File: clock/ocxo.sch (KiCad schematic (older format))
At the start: 50 parts, among them Q201 MMBT3904, U201 PCA9306, U202 DAC8830, U203 LMV722, U204 LTC2990, U205 LP3853, U207 NC7SZ125, Y202 CX210

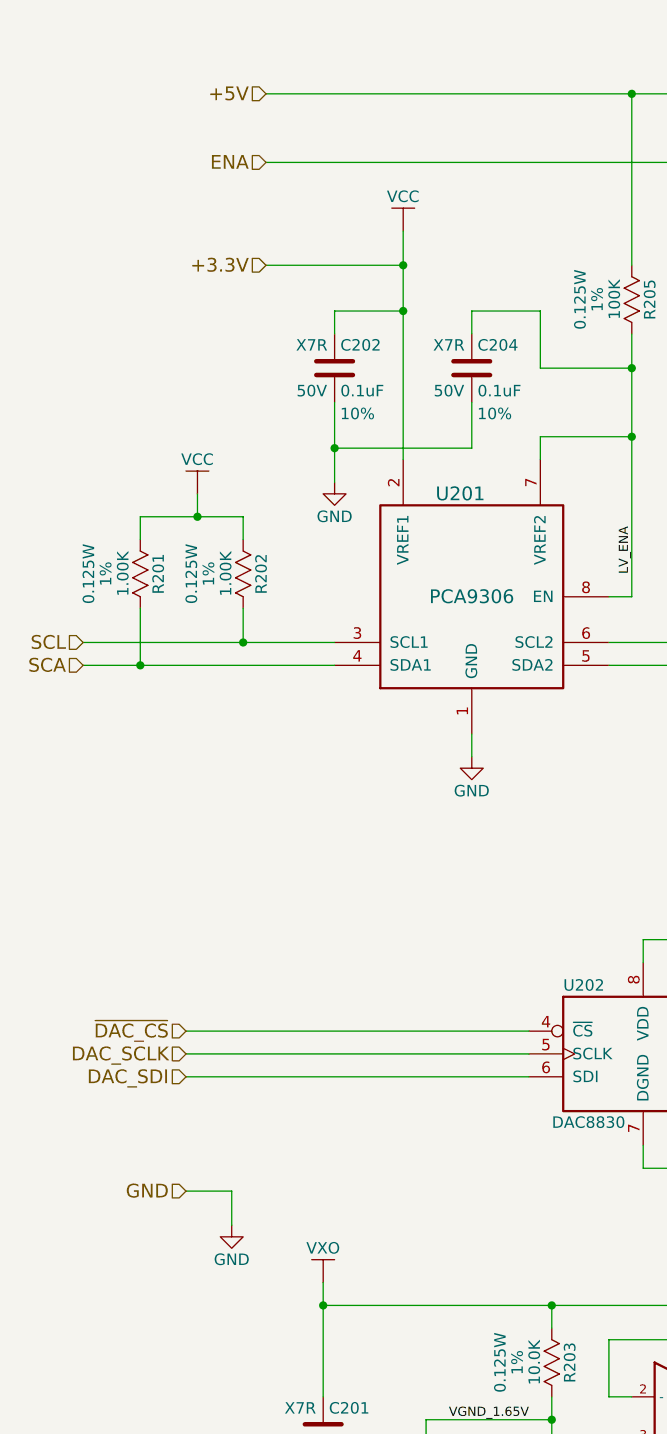
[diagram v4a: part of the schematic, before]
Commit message: Remove sheet to sheet power interconnect because power symbols are global.
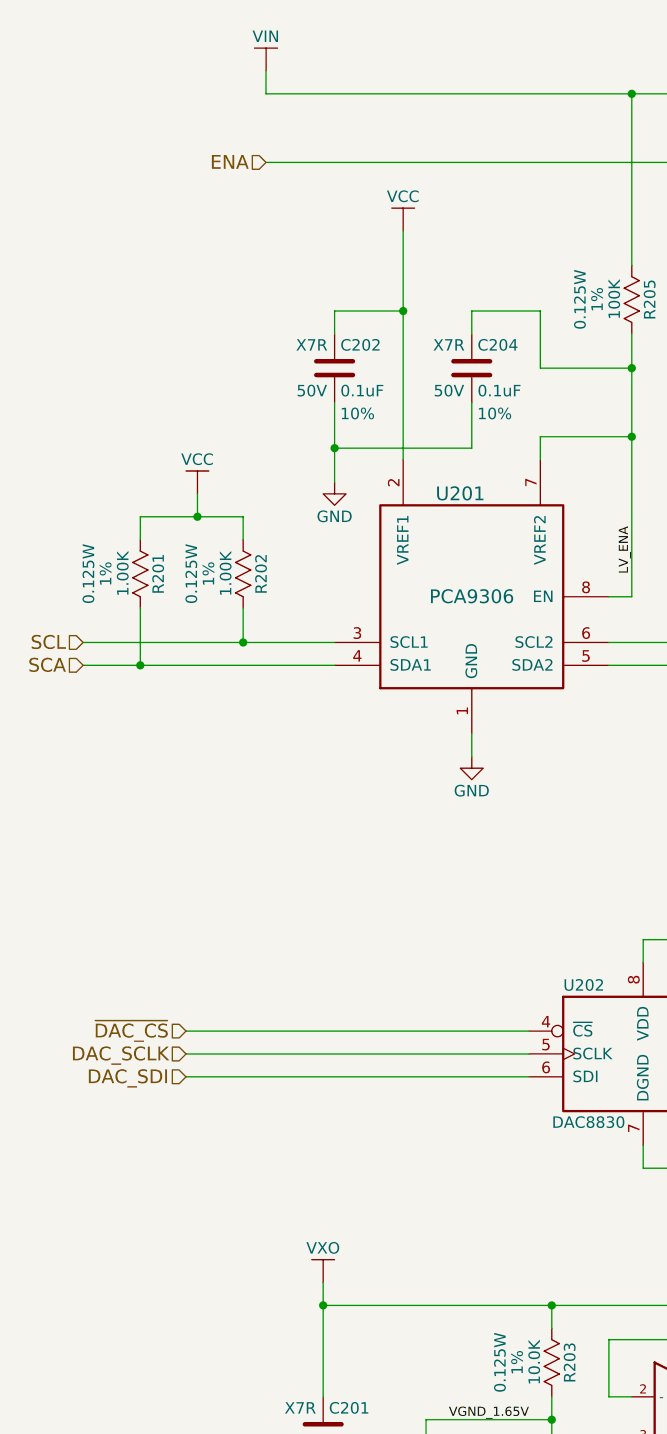
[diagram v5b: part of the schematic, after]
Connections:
- net +5V renamed VIN
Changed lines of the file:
@@
 Comment4 ""
 $EndDescr
-Text HLabel 1650 1000 0    60   Input ~ 0
-+5V
-Text HLabel 1300 5800 0    60   Input ~ 0
-GND
-$Comp
-L GND #PWR222
+$Comp
+L GND #PWR010
 U 1 1 5622D09D
 P 8800 2250
-F 0 "#PWR222" H 8800 2000 50  0001 C CNN
+F 0 "#PWR010" H 8800 2000 50  0001 C CNN
 F 1 "GND" H 8800 2100 50  0000 C CNN
 F 2 "" H 8800 2250 60  0000 C CNN
@@
 	1    0    0    -1
 $EndComp
-Text HLabel 1650 1750 0    60   Input ~ 0
-+3.3V
 Text HLabel 850  3400 0    60   Input ~ 0
 SCL
@@
 ENA
 $Comp
-L GND #PWR204
+L GND #PWR011
 U 1 1 5622E675
 P 1950 2700
-F 0 "#PWR204" H 1950 2450 50  0001 C CNN
+F 0 "#PWR011" H 1950 2450 50  0001 C CNN
 F 1 "GND" H 1950 2550 50  0000 C CNN
 F 2 "" H 1950 2700 60  0000 C CNN
@@
 $EndComp
 $Comp
-L GND #PWR211
+L GND #PWR012
 U 1 1 5622EAE9
 P 4750 2300
-F 0 "#PWR211" H 4750 2050 50  0001 C CNN
+F 0 "#PWR012" H 4750 2050 50  0001 C CNN
 F 1 "GND" H 4750 2150 50  0000 C CNN
 F 2 "" H 4750 2300 60  0000 C CNN
@@
 $EndComp
 $Comp
-L GND #PWR213
+L GND #PWR013
 U 1 1 5622ED34
 P 5500 3500
-F 0 "#PWR213" H 5500 3250 50  0001 C CNN
+F 0 "#PWR013" H 5500 3250 50  0001 C CNN
 F 1 "GND" H 5500 3350 50  0000 C CNN
 F 2 "" H 5500 3500 60  0000 C CNN
@@
 $EndComp
 $Comp
-L GND #PWR206
+L GND #PWR014
 U 1 1 5622EF10
 P 2550 3900
-F 0 "#PWR206" H 2550 3650 50  0001 C CNN
+F 0 "#PWR014" H 2550 3650 50  0001 C CNN
 F 1 "GND" H 2550 3750 50  0000 C CNN
 F 2 "" H 2550 3900 60  0000 C CNN
@@
 $EndComp
 $Comp
-L GND #PWR212
+L GND #PWR015
 U 1 1 5622FB6A
 P 4750 7550
-F 0 "#PWR212" H 4750 7300 50  0001 C CNN
+F 0 "#PWR015" H 4750 7300 50  0001 C CNN
 F 1 "GND" H 4750 7400 50  0000 C CNN
 F 2 "" H 4750 7550 60  0000 C CNN
@@
 $EndComp
 $Comp
-L GND #PWR208
+L GND #PWR016
 U 1 1 56230FF6
 P 3500 5800
-F 0 "#PWR208" H 3500 5550 50  0001 C CNN
+F 0 "#PWR016" H 3500 5550 50  0001 C CNN
 F 1 "GND" H 3500 5650 50  0000 C CNN
 F 2 "" H 3500 5800 60  0000 C CNN
@@
 $EndComp
 $Comp
-L GND #PWR219
+L GND #PWR017
 U 1 1 5623121C
 P 7750 6200
-F 0 "#PWR219" H 7750 5950 50  0001 C CNN
+F 0 "#PWR017" H 7750 5950 50  0001 C CNN
 F 1 "GND" H 7750 6050 50  0000 C CNN
 F 2 "" H 7750 6200 60  0000 C CNN
@@
 $EndComp
 $Comp
-L GND #PWR215
+L GND #PWR018
 U 1 1 56231287
 P 5850 6100
-F 0 "#PWR215" H 5850 5850 50  0001 C CNN
+F 0 "#PWR018" H 5850 5850 50  0001 C CNN
 F 1 "GND" H 5850 5950 50  0000 C CNN
 F 2 "" H 5850 6100 60  0000 C CNN
@@
 DAC_SDI
 $Comp
-L GND #PWR221
+L GND #PWR019
 U 1 1 562345F5
 P 8400 4750
-F 0 "#PWR221" H 8400 4500 50  0001 C CNN
+F 0 "#PWR019" H 8400 4500 50  0001 C CNN
 F 1 "GND" H 8400 4600 50  0000 C CNN
 F 2 "" H 8400 4750 60  0000 C CNN
@@
 $EndComp
 $Comp
-L GND #PWR210
+L GND #PWR020
 U 1 1 5623BD4E
 P 3950 4800
-F 0 "#PWR210" H 3950 4550 50  0001 C CNN
+F 0 "#PWR020" H 3950 4550 50  0001 C CNN
 F 1 "GND" H 3950 4650 50  0000 C CNN
 F 2 "" H 3950 4800 60  0000 C CNN
@@
 $EndComp
 $Comp
-L VXO #PWR230
+L VXO #PWR021
 U 1 1 56247A78
 P 10800 1150
-F 0 "#PWR230" H 10800 1000 50  0001 C CNN
+F 0 "#PWR021" H 10800 1000 50  0001 C CNN
 F 1 "VXO" H 10800 1300 50  0000 C CNN
 F 2 "" H 10800 1150 60  0000 C CNN
@@
 $EndComp
 $Comp
-L VXO #PWR214
+L VXO #PWR022
 U 1 1 562483EB
 P 5850 5050
-F 0 "#PWR214" H 5850 4900 50  0001 C CNN
+F 0 "#PWR022" H 5850 4900 50  0001 C CNN
 F 1 "VXO" H 5850 5200 50  0000 C CNN
 F 2 "" H 5850 5050 60  0000 C CNN
@@
 $EndComp
 $Comp
-L VXO #PWR207
+L VXO #PWR023
 U 1 1 562484D6
 P 3500 4500
-F 0 "#PWR207" H 3500 4350 50  0001 C CNN
+F 0 "#PWR023" H 3500 4350 50  0001 C CNN
 F 1 "VXO" H 3500 4650 50  0000 C CNN
 F 2 "" H 3500 4500 60  0000 C CNN
@@
 $EndComp
 $Comp
-L VXO #PWR209
+L VXO #PWR024
 U 1 1 56248541
 P 3950 4300
-F 0 "#PWR209" H 3950 4150 50  0001 C CNN
+F 0 "#PWR024" H 3950 4150 50  0001 C CNN
 F 1 "VXO" H 3950 4450 50  0000 C CNN
 F 2 "" H 3950 4300 60  0000 C CNN
@@
 $EndComp
 $Comp
-L VXO #PWR203
+L VXO #PWR025
 U 1 1 56248C4D
 P 1900 6200
-F 0 "#PWR203" H 1900 6050 50  0001 C CNN
+F 0 "#PWR025" H 1900 6050 50  0001 C CNN
 F 1 "VXO" H 1900 6350 50  0000 C CNN
 F 2 "" H 1900 6200 60  0000 C CNN
@@
 	1    0    0    -1
 $EndComp
-$Comp
-L GND #PWR202
-U 1 1 5624901D
-P 1500 5950
-F 0 "#PWR202" H 1500 5700 50  0001 C CNN
-F 1 "GND" H 1500 5800 50  0000 C CNN
-F 2 "" H 1500 5950 60  0000 C CNN
-F 3 "" H 1500 5950 60  0000 C CNN
-	1    1500 5950
-	1    0    0    -1
-$EndComp
 Wire Wire Line
 	1650 1300 6550 1300
@@
 Connection ~ 10000 2150
 Wire Wire Line
-	1650 1750 2250 1750
-Wire Wire Line
 	2250 1600 2250 2600
 Wire Wire Line
@@
 	3950 4300 3950 4400
 Connection ~ 1900 6300
-Wire Wire Line
-	1500 5800 1500 5950
-Wire Wire Line
-	1300 5800 1500 5800
 Wire Wire Line
 	5850 5400 5850 5050
@@
 $EndComp
 $Comp
-L GND #PWR225
+L GND #PWR026
 U 1 1 56356688
 P 9300 2600
-F 0 "#PWR225" H 9300 2350 50  0001 C CNN
+F 0 "#PWR026" H 9300 2350 50  0001 C CNN
 F 1 "GND" H 9300 2450 50  0000 C CNN
 F 2 "" H 9300 2600 60  0000 C CNN
@@
 $EndComp
 $Comp
-L GND #PWR226
+L GND #PWR027
 U 1 1 563568AD
 P 9900 2600
-F 0 "#PWR226" H 9900 2350 50  0001 C CNN
+F 0 "#PWR027" H 9900 2350 50  0001 C CNN
 F 1 "GND" H 9900 2450 50  0000 C CNN
 F 2 "" H 9900 2600 60  0000 C CNN
@@
 	9300 2500 9300 2600
 $Comp
-L GND #PWR220
+L GND #PWR028
 U 1 1 5636F400
 P 8300 6200
-F 0 "#PWR220" H 8300 5950 50  0001 C CNN
+F 0 "#PWR028" H 8300 5950 50  0001 C CNN
 F 1 "GND" H 8300 6050 50  0000 C CNN
 F 2 "" H 8300 6200 60  0000 C CNN
@@
 $EndComp
 $Comp
-L GND #PWR223
+L GND #PWR029
 U 1 1 56370766
 P 9000 4750
-F 0 "#PWR223" H 9000 4500 50  0001 C CNN
+F 0 "#PWR029" H 9000 4500 50  0001 C CNN
 F 1 "GND" H 9000 4600 50  0000 C CNN
 F 2 "" H 9000 4750 60  0000 C CNN
@@
 	9850 5700 10250 5700
 $Comp
-L VCC #PWR228
+L VCC #PWR030
 U 1 1 563724DA
 P 10450 4550
-F 0 "#PWR228" H 10450 4400 50  0001 C CNN
+F 0 "#PWR030" H 10450 4400 50  0001 C CNN
 F 1 "VCC" H 10450 4700 50  0000 C CNN
 F 2 "" H 10450 4550 60  0000 C CNN
@@
 $EndComp
 $Comp
-L GND #PWR229
+L GND #PWR031
 U 1 1 56372768
 P 10450 5050
-F 0 "#PWR229" H 10450 4800 50  0001 C CNN
+F 0 "#PWR031" H 10450 4800 50  0001 C CNN
 F 1 "GND" H 10450 4900 50  0000 C CNN
 F 2 "" H 10450 5050 60  0000 C CNN
@@
 	10450 4550 10450 4650
 $Comp
-L GND #PWR224
+L GND #PWR032
 U 1 1 56372915
 P 9100 5350
-F 0 "#PWR224" H 9100 5100 50  0001 C CNN
+F 0 "#PWR032" H 9100 5100 50  0001 C CNN
 F 1 "GND" H 9100 5200 50  0000 C CNN
 F 2 "" H 9100 5350 60  0000 C CNN
@@
 	9100 5200 9100 5350
 $Comp
-L VCC #PWR205
+L VCC #PWR033
 U 1 1 56372BE4
 P 2250 1600
-F 0 "#PWR205" H 2250 1450 50  0001 C CNN
+F 0 "#PWR033" H 2250 1450 50  0001 C CNN
 F 1 "VCC" H 2250 1750 50  0000 C CNN
 F 2 "" H 2250 1600 60  0000 C CNN
@@
 	1    0    0    -1
 $EndComp
-Connection ~ 2250 1750
 $Comp
 L NC7SZ125 U207
@@
 	1550 2850 1550 2950
 $Comp
-L VCC #PWR201
+L VCC #PWR034
 U 1 1 56383EBC
 P 1350 2750
-F 0 "#PWR201" H 1350 2600 50  0001 C CNN
+F 0 "#PWR034" H 1350 2600 50  0001 C CNN
 F 1 "VCC" H 1350 2900 50  0000 C CNN
 F 2 "" H 1350 2750 60  0000 C CNN
@@
 Connection ~ 9000 4250
 $Comp
-L VXO #PWR227
+L VXO #PWR035
 U 1 1 56416BAD
 P 10000 4150
-F 0 "#PWR227" H 10000 4000 50  0001 C CNN
+F 0 "#PWR035" H 10000 4000 50  0001 C CNN
 F 1 "VXO" H 10000 4300 50  0000 C CNN
 F 2 "" H 10000 4150 60  0000 C CNN
@@
 FILT_VXO
 $Comp
-L PWR_FLAG #FLG201
+L PWR_FLAG #FLG036
 U 1 1 56436E86
 P 6750 900
-F 0 "#FLG201" H 6750 995 50  0001 C CNN
+F 0 "#FLG036" H 6750 995 50  0001 C CNN
 F 1 "PWR_FLAG" H 6750 1080 50  0000 C CNN
 F 2 "" H 6750 900 60  0000 C CNN
@@
 Connection ~ 6750 1000
 $Comp
-L PWR_FLAG #FLG202
+L PWR_FLAG #FLG037
 U 1 1 56437DD8
 P 8700 4100
-F 0 "#FLG202" H 8700 4195 50  0001 C CNN
+F 0 "#FLG037" H 8700 4195 50  0001 C CNN
 F 1 "PWR_FLAG" H 8700 4280 50  0000 C CNN
 F 2 "" H 8700 4100 60  0000 C CNN
@@
 	7550 1000 7550 1650
 $Comp
-L GND #PWR216
+L GND #PWR038
 U 1 1 57AABB86
 P 6550 2150
-F 0 "#PWR216" H 6550 1900 50  0001 C CNN
+F 0 "#PWR038" H 6550 1900 50  0001 C CNN
 F 1 "GND" H 6550 2000 50  0000 C CNN
 F 2 "" H 6550 2150 60  0000 C CNN
@@
 Connection ~ 7050 5700
 $Comp
-L GND #PWR217
+L GND #PWR039
 U 1 1 57C04413
 P 7050 6200
-F 0 "#PWR217" H 7050 5950 50  0001 C CNN
+F 0 "#PWR039" H 7050 5950 50  0001 C CNN
 F 1 "GND" H 7050 6050 50  0000 C CNN
 F 2 "" H 7050 6200 60  0000 C CNN
@@
 	7250 4650 7250 4750
 $Comp
-L GND #PWR218
+L GND #PWR040
 U 1 1 589807A7
 P 7250 5250
-F 0 "#PWR218" H 7250 5000 50  0001 C CNN
+F 0 "#PWR040" H 7250 5000 50  0001 C CNN
 F 1 "GND" H 7250 5100 50  0000 C CNN
 F 2 "" H 7250 5250 60  0000 C CNN
@@
 	7250 4250 7250 4350
 Connection ~ 7750 4250
+$Comp
+L VIN #PWR041
+U 1 1 58984F98
+P 1650 900
+F 0 "#PWR041" H 1650 750 50  0001 C CNN
+F 1 "VIN" H 1650 1050 50  0000 C CNN
+F 2 "" H 1650 900 60  0000 C CNN
+F 3 "" H 1650 900 60  0000 C CNN
+	1    1650 900
+	1    0    0    -1
+$EndComp
+Wire Wire Line
+	1650 1000 1650 900
 $EndSCHEMATC

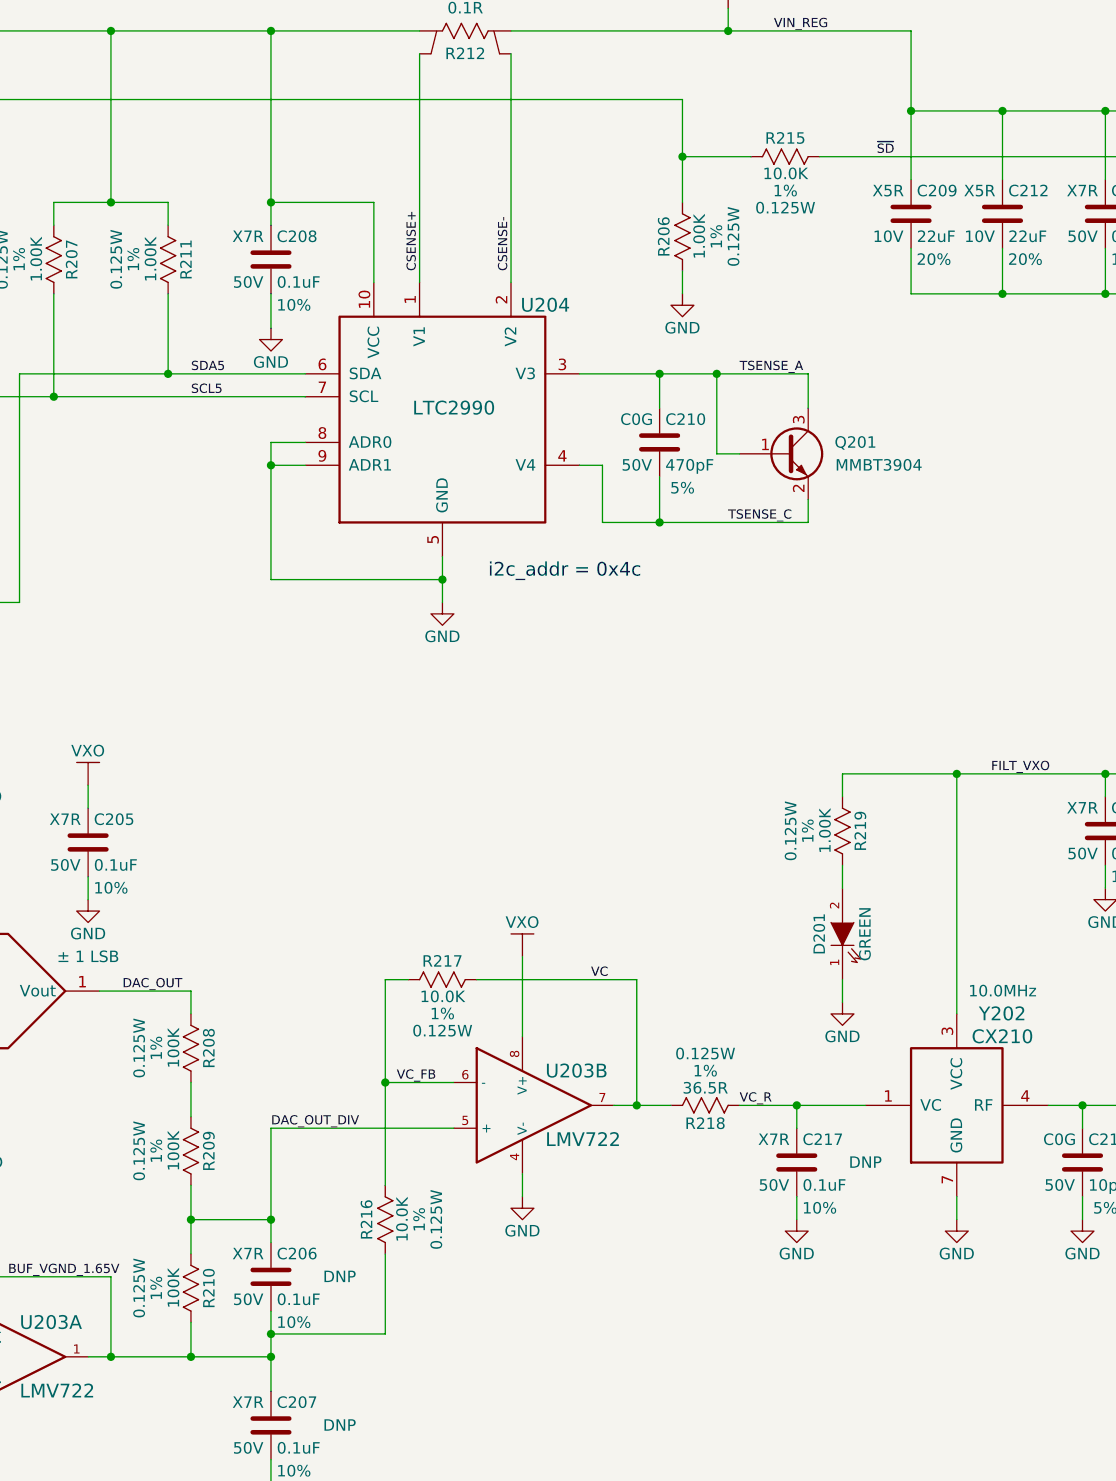
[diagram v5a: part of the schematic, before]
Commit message: Change schematic values to "as built". Regenerate pdf schematic.
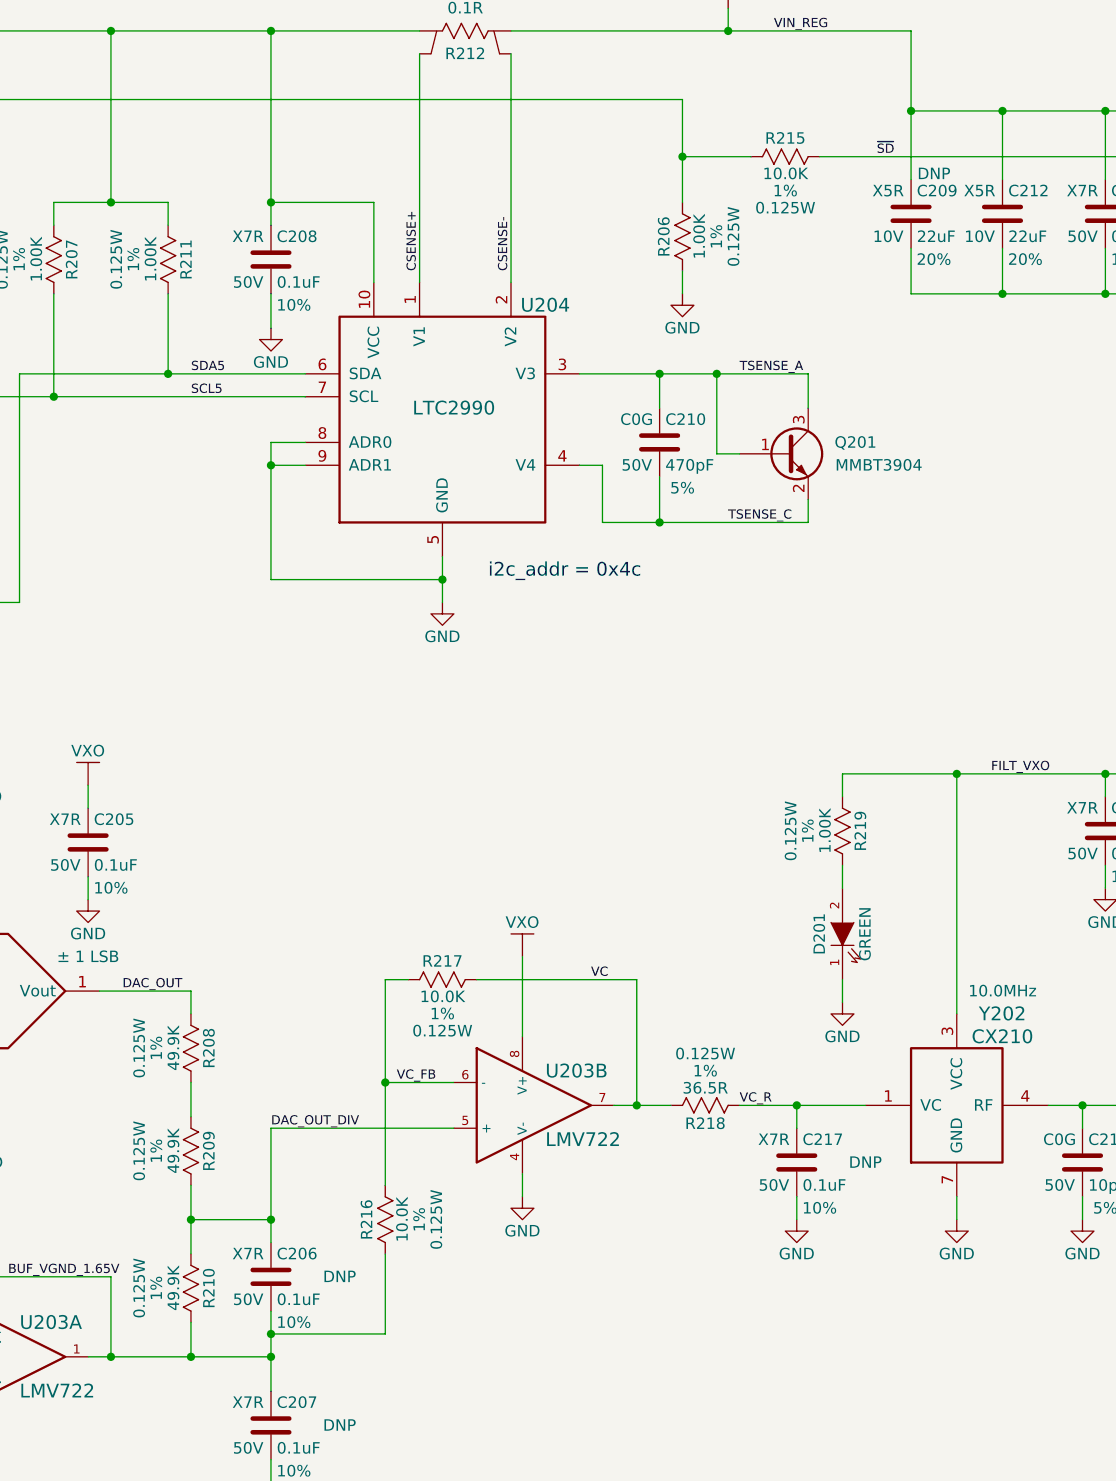
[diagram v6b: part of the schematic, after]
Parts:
- C209: DNP (none) -> DNP
- R208, R209, R210: value 100K -> 49.9K; PartNum CRCW0805100KFKEA -> CRCW080549K9FKEA
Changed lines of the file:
@@
 P 4400 5450
 F 0 "R208" V 4480 5450 50  0000 C CNN
-F 1 "100K" V 4325 5450 50  0000 C CNN
+F 1 "49.9K" V 4325 5450 50  0000 C CNN
 F 2 "local:R_0805_HandSoldering" V 4330 5450 30  0001 C CNN
 F 3 "" V 4480 5450 30  0000 C CNN
@@
 F 5 "0.125W" V 4175 5450 50  0000 C CNN "Power"
 F 6 "Vishay Dale" V 4400 5450 50  0001 C CNN "Manufacturer"
-F 7 "CRCW0805100KFKEA" V 4550 5450 50  0001 C CNN "PartNum"
+F 7 "CRCW080549K9FKEA" V 4550 5450 50  0001 C CNN "PartNum"
 	1    4400 5450
 	1    0    0    -1
@@
 P 4400 5900
 F 0 "R209" V 4480 5900 50  0000 C CNN
-F 1 "100K" V 4325 5900 50  0000 C CNN
+F 1 "49.9K" V 4325 5900 50  0000 C CNN
 F 2 "local:R_0805_HandSoldering" V 4330 5900 30  0001 C CNN
 F 3 "" V 4480 5900 30  0000 C CNN
@@
 F 5 "0.125W" V 4175 5900 50  0000 C CNN "Power"
 F 6 "Vishay Dale" V 4400 5900 50  0001 C CNN "Manufacturer"
-F 7 "CRCW0805100KFKEA" V 4550 5900 50  0001 C CNN "PartNum"
+F 7 "CRCW080549K9FKEA" V 4550 5900 50  0001 C CNN "PartNum"
 	1    4400 5900
 	1    0    0    -1
@@
 P 4400 6500
 F 0 "R210" V 4480 6500 50  0000 C CNN
-F 1 "100K" V 4325 6500 50  0000 C CNN
+F 1 "49.9K" V 4325 6500 50  0000 C CNN
 F 2 "local:R_0805_HandSoldering" V 4330 6500 30  0001 C CNN
 F 3 "" V 4480 6500 30  0000 C CNN
@@
 F 5 "0.125W" V 4175 6500 50  0000 C CNN "Power"
 F 6 "Vishay Dale" V 4400 6500 50  0001 C CNN "Manufacturer"
-F 7 "CRCW0805100KFKEA" V 4550 6500 50  0001 C CNN "PartNum"
+F 7 "CRCW080549K9FKEA" V 4550 6500 50  0001 C CNN "PartNum"
 	1    4400 6500
 	1    0    0    -1
@@
 F 7 "TDK" H 7550 1800 50  0001 C CNN "Manufacturer"
 F 8 "C3216X5R1A226M160AC" H 7550 1800 60  0001 C CNN "PartNum"
+F 9 "DNP" H 7650 1975 50  0000 C CNN "DNP"
 	1    7550 1800
 	1    0    0    -1

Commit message: Update clock board to kicad 5.1. Regenerate output files.
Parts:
- A201: symbol CX210_Cover -> Local:CX210_Cover
- C201, C202, C203, C204, C205, C206, C207, C208, C209, C210, C211, C212, C213, C214, C215, C216, C217, C218, C219: symbol C -> Device:C
- D201: symbol LED -> Local:LED
- FB201: symbol FILTER -> Device:Ferrite_Bead
- HS201: symbol TO220_heatsink -> Local:TO220_heatsink
- Q201: symbol Q_NPN_BEC -> Transistor_BJT:MMBT3904
- R201, R202, R203, R204, R205, R206, R207, R208, R209, R210, R211, R213, R214, R215, R216, R217, R218, R219: symbol R_local -> Local:R_local
- R212: symbol R_CSM2512 -> Local:R_CSM2512
- U201: symbol PCA9306 -> Local:PCA9306
- U202: symbol DAC8830 -> Local:DAC8830
- U203: symbol LMV722 -> Local:LMV722
- U204: symbol LTC2990 -> Local:LTC2990
- U205: symbol LP3853 -> Local:LP3853
- U207: symbol NC7SZ125 -> Local:NC7SZ125
- Y202: symbol CX210 -> Local:CX210
